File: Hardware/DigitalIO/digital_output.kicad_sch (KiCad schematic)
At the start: 40 parts, among them Q10 PMOS, Q11 PMOS, Q12 PMOS, Q13 PMOS, Q14 PMOS, Q15 PMOS, Q16 PMOS, Q17 PMOS, U14 CNY17-4, U15 CNY17-4, U16 CNY17-4, U17 CNY17-4, U18 CNY17-4, U19 CNY17-4, U20 CNY17-4, U21 CNY17-4

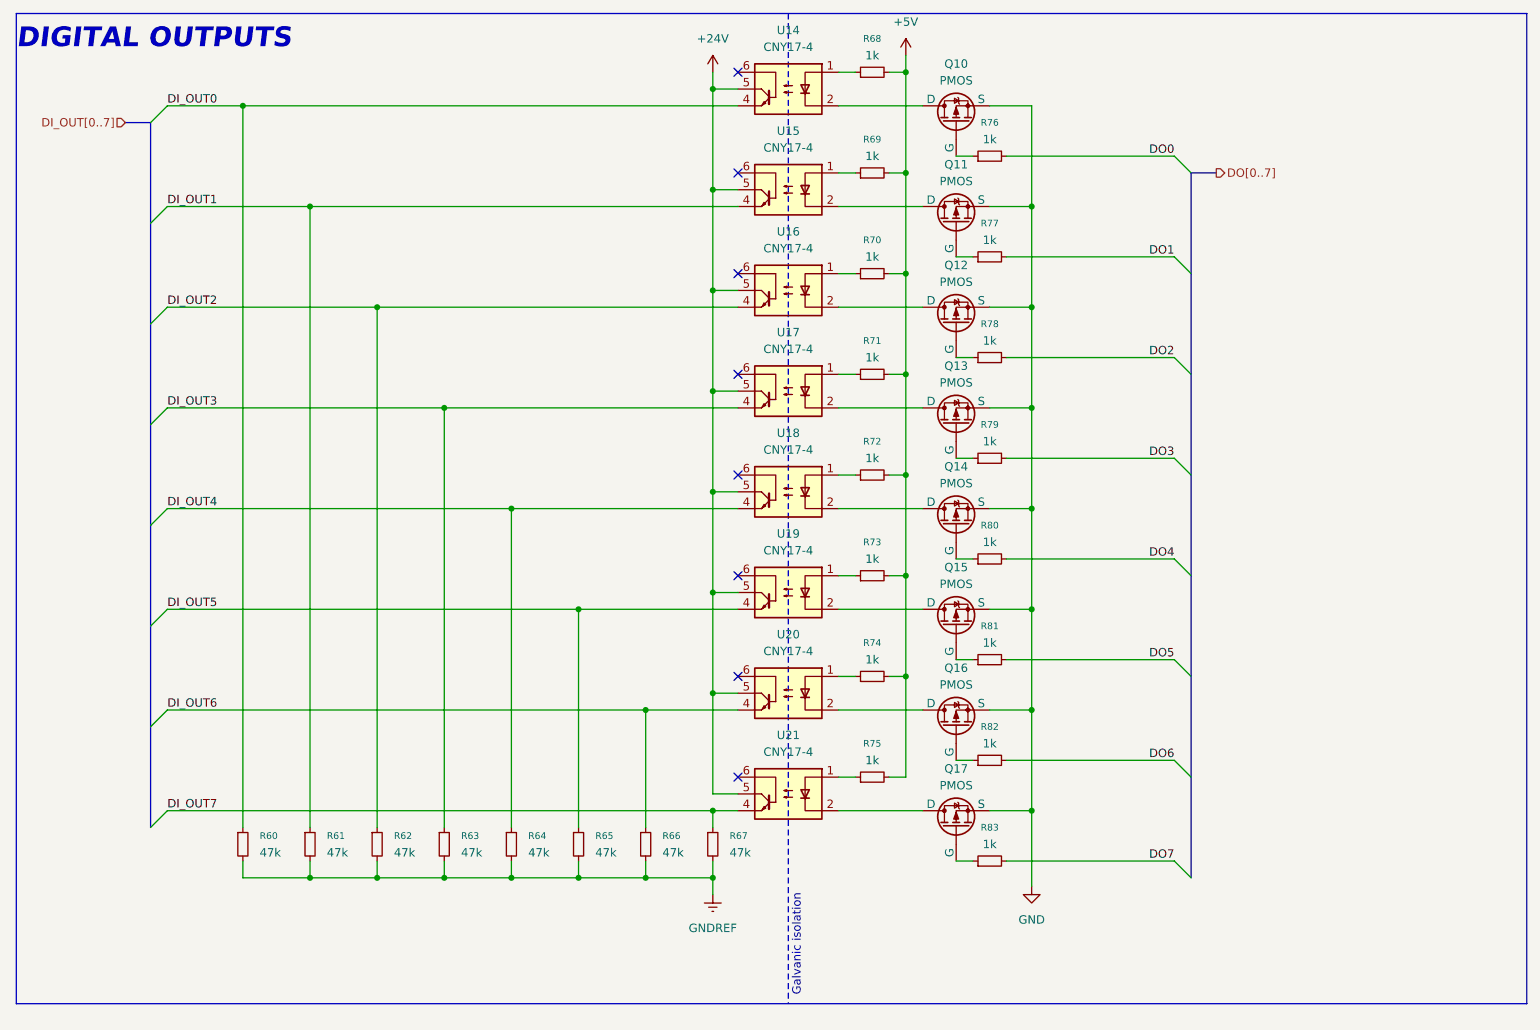
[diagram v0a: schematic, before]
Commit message: schematic update - all pcbs
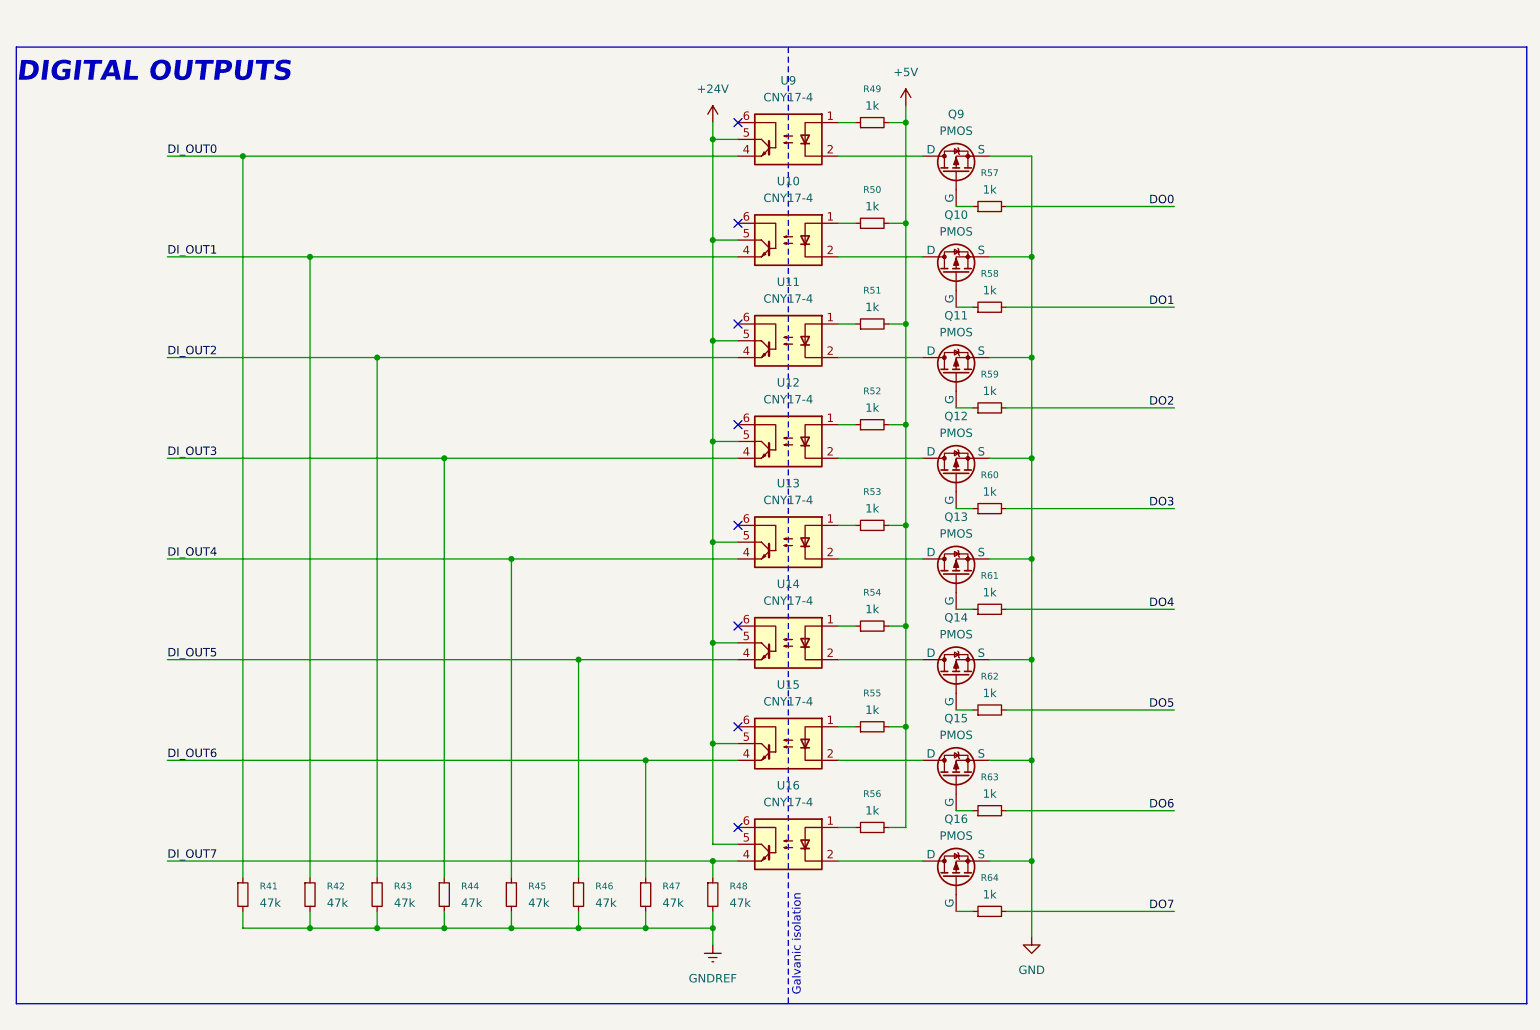
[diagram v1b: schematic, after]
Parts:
- renumbered Q11 to Q10, Q12 to Q11, Q13 to Q12, Q14 to Q13, Q15 to Q14, Q16 to Q15, Q17 to Q16, Q10 to Q9, R60 to R41, R61 to R42, R62 to R43, R63 to R44, R64 to R45, R65 to R46, R66 to R47, R67 to R48, R68 to R49, R69 to R50, R70 to R51, R71 to R52, R72 to R53, R73 to R54, R74 to R55, R75 to R56, R76 to R57, R77 to R58, R78 to R59, R79 to R60, R80 to R61, R81 to R62, R82 to R63, R83 to R64, U15 to U10, U16 to U11, U17 to U12, U18 to U13, U19 to U14, U20 to U15, U21 to U16, U14 to U9
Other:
- moved on the sheet: Q10, Q11, Q12, Q13, Q14, Q15, Q16, Q9, R41, R42, R43, R44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

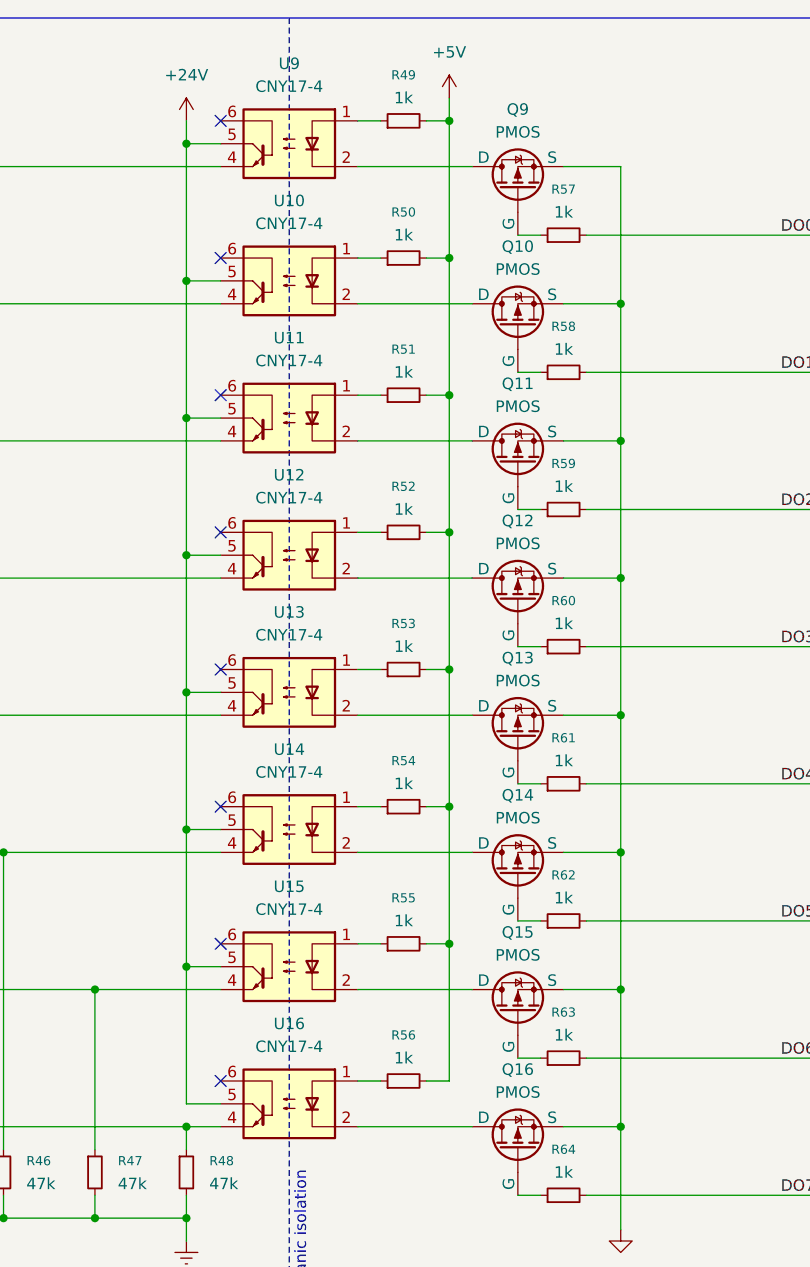
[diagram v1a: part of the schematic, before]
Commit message: schematic update - digital and analog footprints added
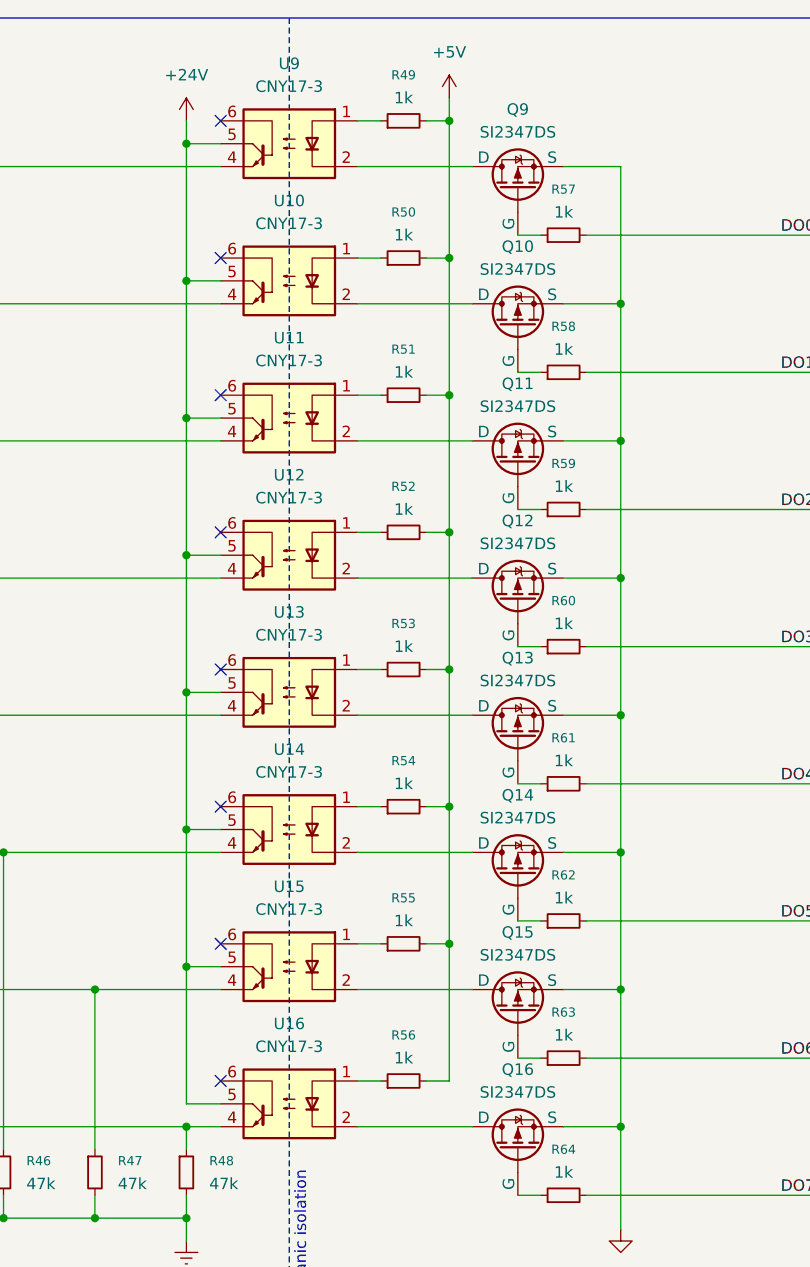
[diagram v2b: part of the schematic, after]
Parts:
- removed U10, U11, U12, U13, U14, U15, U16, U9: CNY17-4, symbol Isolator:CNY17-4
- added U10, U11, U12, U13, U14, U15, U16, U9: CNY17-3, PLC_STM:SOP254P1016X400-6N, symbol Isolator:CNY17-3
- Q10, Q11, Q12, Q13, Q14, Q15, Q16, Q9: value PMOS -> SI2347DS; footprint (none) -> Package_TO_SOT_SMD:SOT-23-3; Mouser Part Number (none) -> 78-SI2347DS-T1-GE3; Mouser Price/Stock (none) -> https://www.mouser.pl/ProductDetail/Vishay-Semiconductors/S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
- R41, R42, R43, R44, R45, R46, R47, R48: footprint (none) -> Resistor_SMD:R_0603_1608Metric_Pad0.98x0.95mm_HandSolder; Mouser Part Number (none) -> 71-CRCW0603-47K-E3; Mouser Price/Stock (none) -> https://www.mouser.pl/ProductDetail/Vishay/CRCW060347K0FKEA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
- R49, R50, R51, R52, R53, R54, R55, R56, R57, R58, R59, R60, R61, R62, R63, R64: footprint (none) -> Resistor_SMD:R_0603_1608Metric_Pad0.98x0.95mm_HandSolder; Mouser Part Number (none) -> 71-CRCW06031K00FKED; Mouser Price/Stock (none) -> https://www.mouser.pl/ProductDetail/Vishay/CRCW06031K00FKED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
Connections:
- net +24V: now also U10.5, U11.5, U12.5, U13.5, U14.5, U15.5, U16.5, U9.5
- net DI_OUT0: now also U9.4
- net DI_OUT1: now also U10.4
- net DI_OUT2: now also U11.4
- net DI_OUT3: now also U12.4
- net DI_OUT4: now also U13.4
- net DI_OUT5: now also U14.4
- net DI_OUT6: now also U15.4
- net DI_OUT7: now also U16.4
- net at R53.1: now also U13.1
- net at Q13.1 (D): now also U13.2
- net at Q12.1 (D): now also U12.2
- net at R49.1: now also U9.1
- net at Q9.1 (D): now also U9.2
- net at Q15.1 (D): now also U15.2
- net at Q10.1 (D): now also U10.2
- net at R50.1: now also U10.1
- net at R52.1: now also U12.1
- net at R56.1: now also U16.1
- net at Q16.1 (D): now also U16.2
- net at R55.1: now also U15.1
- net at R54.1: now also U14.1
- net at Q14.1 (D): now also U14.2
- net at R51.1: now also U11.1
- net at Q11.1 (D): now also U11.2
